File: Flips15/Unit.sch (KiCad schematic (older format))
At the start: 2 parts, among them U201 74LS138

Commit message: rework Flips15 draft
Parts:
- removed U201: 74LS138, SMD_Packages:SO-16-N, symbol 74xx_IEEE:74LS138
- added U201: 74HC238, Housings_SOIC:SOIC-16_3.9x9.9mm_Pitch1.27mm, symbol 74xx_IEEE:74HC238
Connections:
- net B0: now also U201.2 (A1)
- net B1: now also U201.3 (A2)
- net DATA: now also U201.1 (A0)
- net EN: now also U201.6 (G1)
- net GND: now also U201.4 (~G2A), U201.5 (~G2B), U201.8 (GND)
- net VCC: now also U201.16 (VCC)
- new net E0H: U201.14 (Y1)
- new net E0L: U201.15 (Y0)
- new net E1H: U201.12 (Y3)
- new net E1L: U201.13 (Y2)
- new net E2H: U201.10 (Y5)
- new net E2L: U201.11 (Y4)
- new net E3H: U201.7 (Y7)
- new net E3L: U201.9 (Y6)
- no-connect marks 4 -> 0

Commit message: more silk screen (use more compact IC values)
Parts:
- U201: value 74HC238 -> 74238
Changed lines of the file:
@@
 AR Path="/5C4DA960/5C55B425" Ref="U701"  Part="1"
 F 0 "U701" H 2700 5616 50  0000 C CNN
-F 1 "74HC238" H 2700 5525 50  0000 C CNN
+F 1 "74238" H 2700 5525 50  0000 C CNN
 F 2 "Housings_SOIC:SOIC-16_3.9x9.9mm_Pitch1.27mm" H 2700 5100 50  0001 C CNN
 F 3 "" H 2700 5100 50  0001 C CNN

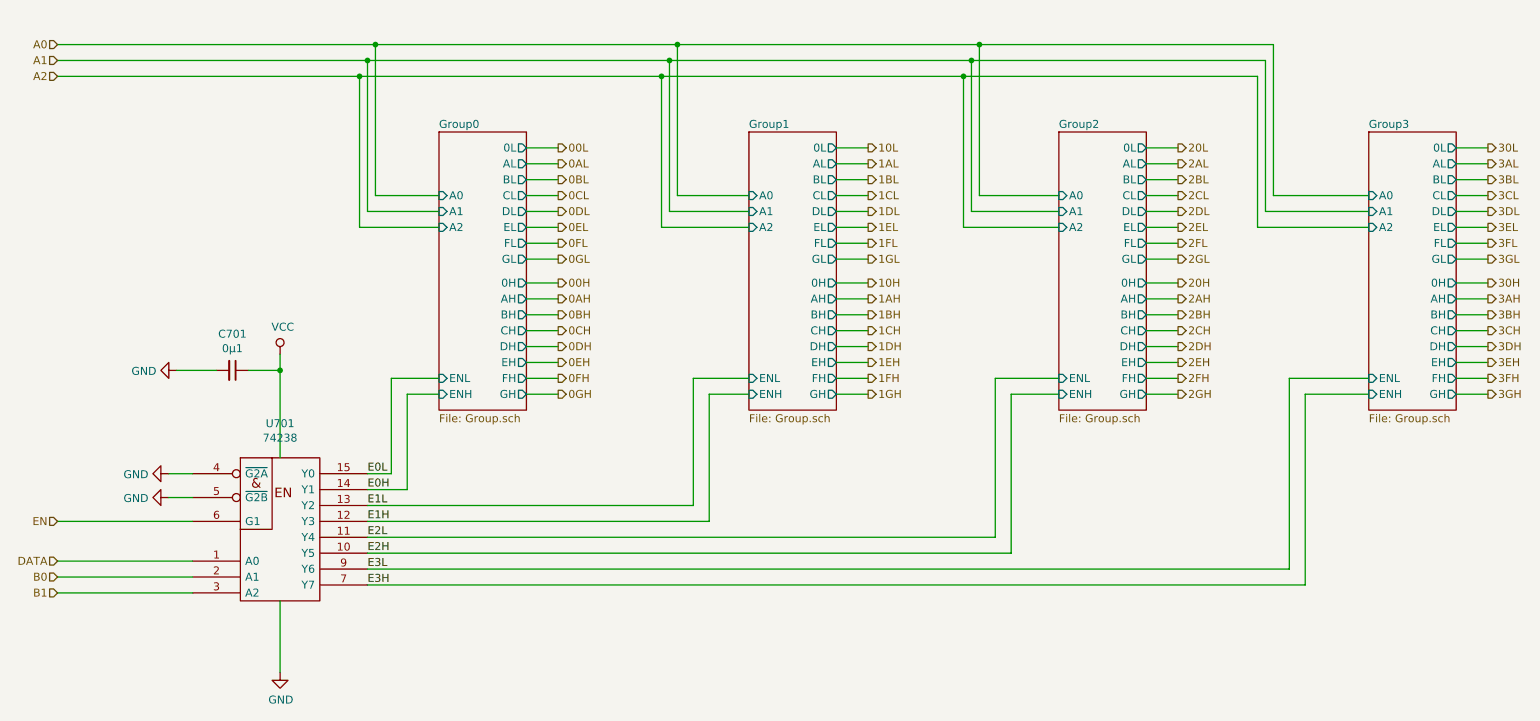
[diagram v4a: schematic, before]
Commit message: adding support for optional COM pin at BRDIC1
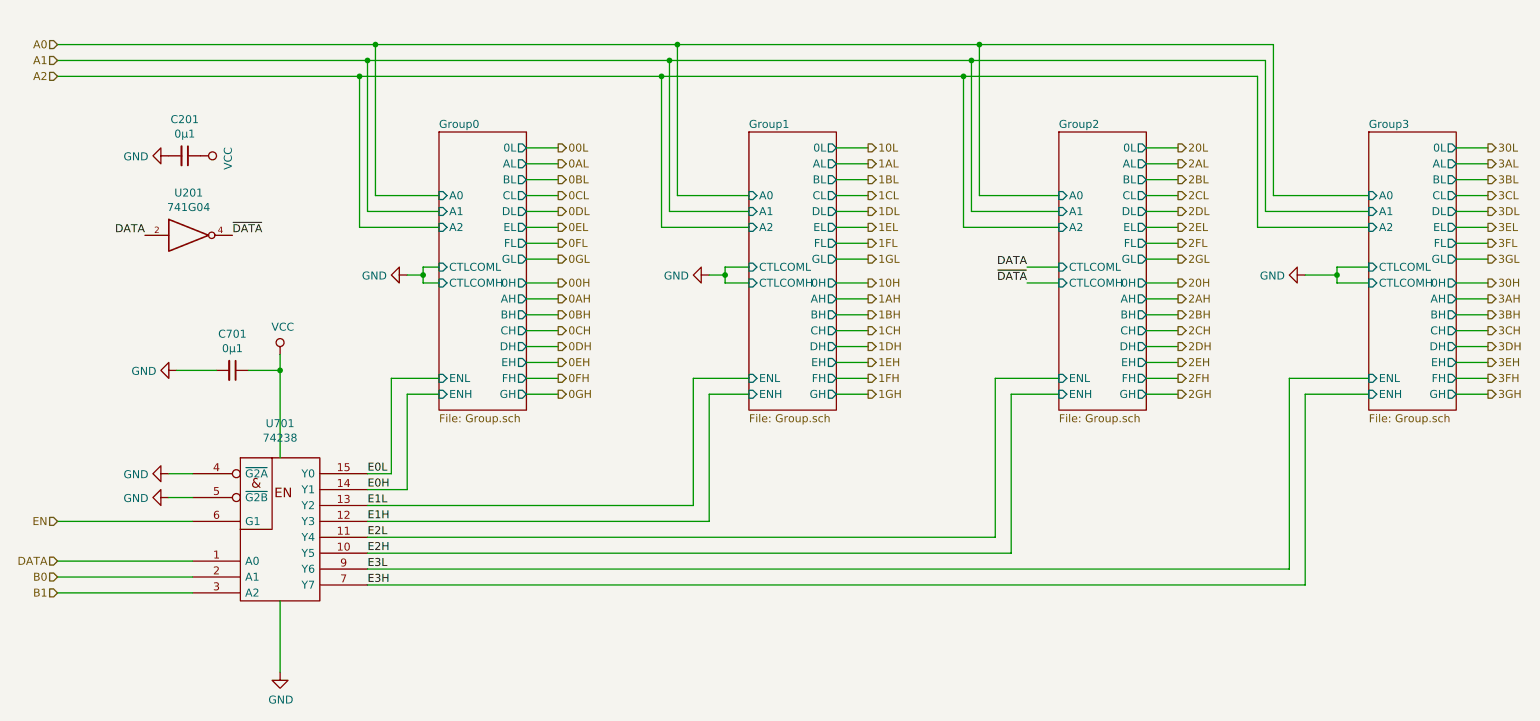
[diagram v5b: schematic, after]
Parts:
- added C201: 0μ1, Capacitors_SMD:C_0805_HandSoldering, symbol Device:C_Small
- added U201: 741G04, TO_SOT_Packages_SMD:SOT-23-5, symbol 74xGxx:74LVC1G04
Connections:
- net DATA: now also U201.2
- net GND: now also C201.2, U201.3 (GND)
- net VCC: now also C201.1, U201.5 (VCC)
- new net ~DATA: U201.4
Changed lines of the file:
@@
 F21 "ENH" I L 3700 4400 50
 F22 "ENL" I L 3700 4300 50
+F23 "CTLCOML" I L 3700 3600 50
+F24 "CTLCOMH" I L 3700 3700 50
 $EndSheet
 $Sheet
@@
 F21 "ENH" I L 5650 4400 50
 F22 "ENL" I L 5650 4300 50
+F23 "CTLCOML" I L 5650 3600 50
+F24 "CTLCOMH" I L 5650 3700 50
 $EndSheet
 $Sheet
@@
 F21 "ENH" I L 7600 4400 50
 F22 "ENL" I L 7600 4300 50
+F23 "CTLCOML" I L 7600 3600 50
+F24 "CTLCOMH" I L 7600 3700 50
 $EndSheet
 $Sheet
@@
 F21 "ENH" I L 9550 4400 50
 F22 "ENL" I L 9550 4300 50
+F23 "CTLCOML" I L 9550 3600 50
+F24 "CTLCOMH" I L 9550 3700 50
 $EndSheet
 Wire Wire Line
@@
 Text Label 3250 5600 0    50   ~ 0
 E3H
+$Comp
+L power:GND #PWR?
+U 1 1 5C5C466E
+P 3500 3650
+AR Path="/5C5C466E" Ref="#PWR?"  Part="1"
+AR Path="/5C4DA950/5C5C466E" Ref="#PWR?"  Part="1"
+AR Path="/5C4DA960/5C5C466E" Ref="#PWR0203"  Part="1"
+F 0 "#PWR0203" H 3500 3400 50  0001 C CNN
+F 1 "GND" V 3505 3522 50  0000 R CNN
+F 2 "" H 3500 3650 50  0001 C CNN
+F 3 "" H 3500 3650 50  0001 C CNN
+	1    3500 3650
+	0    1    1    0
+$EndComp
+Wire Wire Line
+	3500 3650 3600 3650
+Wire Wire Line
+	3600 3650 3600 3600
+Wire Wire Line
+	3600 3600 3700 3600
+Wire Wire Line
+	3700 3700 3600 3700
+Wire Wire Line
+	3600 3700 3600 3650
+Connection ~ 3600 3650
+Wire Wire Line
+	5650 3600 5500 3600
+Wire Wire Line
+	5500 3600 5500 3650
+Wire Wire Line
+	5500 3700 5650 3700
+Wire Wire Line
+	5500 3650 5400 3650
+Connection ~ 5500 3650
+Wire Wire Line
+	5500 3650 5500 3700
+$Comp
+L power:GND #PWR?
+U 1 1 5C5E08DC
+P 5400 3650
+AR Path="/5C5E08DC" Ref="#PWR?"  Part="1"
+AR Path="/5C4DA950/5C5E08DC" Ref="#PWR?"  Part="1"
+AR Path="/5C4DA960/5C5E08DC" Ref="#PWR0204"  Part="1"
+F 0 "#PWR0204" H 5400 3400 50  0001 C CNN
+F 1 "GND" V 5405 3522 50  0000 R CNN
+F 2 "" H 5400 3650 50  0001 C CNN
+F 3 "" H 5400 3650 50  0001 C CNN
+	1    5400 3650
+	0    1    1    0
+$EndComp
+Wire Wire Line
+	7400 3700 7600 3700
+Wire Wire Line
+	7600 3600 7400 3600
+Wire Wire Line
+	9550 3600 9350 3600
+Wire Wire Line
+	9350 3600 9350 3650
+Wire Wire Line
+	9350 3700 9550 3700
+Wire Wire Line
+	9350 3650 9150 3650
+Connection ~ 9350 3650
+Wire Wire Line
+	9350 3650 9350 3700
+$Comp
+L power:GND #PWR?
+U 1 1 5C5FF9CF
+P 9150 3650
+AR Path="/5C5FF9CF" Ref="#PWR?"  Part="1"
+AR Path="/5C4DA950/5C5FF9CF" Ref="#PWR?"  Part="1"
+AR Path="/5C4DA960/5C5FF9CF" Ref="#PWR0205"  Part="1"
+F 0 "#PWR0205" H 9150 3400 50  0001 C CNN
+F 1 "GND" V 9155 3522 50  0000 R CNN
+F 2 "" H 9150 3650 50  0001 C CNN
+F 3 "" H 9150 3650 50  0001 C CNN
+	1    9150 3650
+	0    1    1    0
+$EndComp
+Text Label 7400 3600 2    50   ~ 0
+DATA
+Text Label 7400 3700 2    50   ~ 0
+~DATA
+$Comp
+L 74xGxx:74LVC1G04 U201
+U 1 1 5C5FFB09
+P 2150 3400
+F 0 "U201" H 2125 3667 50  0000 C CNN
+F 1 "741G04" H 2125 3576 50  0000 C CNN
+F 2 "TO_SOT_Packages_SMD:SOT-23-5" H 2150 3400 50  0001 C CNN
+F 3 "http://www.ti.com/lit/sg/scyt129e/scyt129e.pdf" H 2150 3400 50  0001 C CNN
+	1    2150 3400
+	1    0    0    -1
+$EndComp
+Text Label 2400 3400 0    50   ~ 0
+~DATA
+Text Label 1850 3400 2    50   ~ 0
+DATA
+$Comp
+L Device:C_Small C?
+U 1 1 5C5FFCA0
+P 2100 2900
+AR Path="/5C4CE2B0/5C5FFCA0" Ref="C?"  Part="1"
+AR Path="/5C5018C5/5C5FFCA0" Ref="C?"  Part="1"
+AR Path="/5C5FFCA0" Ref="C?"  Part="1"
+AR Path="/5C4DA950/5C5FFCA0" Ref="C?"  Part="1"
+AR Path="/5C4DA960/5C5FFCA0" Ref="C201"  Part="1"
+F 0 "C201" V 1871 2900 50  0000 C CNN
+F 1 "0μ1" V 1962 2900 50  0000 C CNN
+F 2 "Capacitors_SMD:C_0805_HandSoldering" H 2100 2900 50  0001 C CNN
+F 3 "~" H 2100 2900 50  0001 C CNN
+	1    2100 2900
+	0    1    1    0
+$EndComp
+$Comp
+L power:GND #PWR?
+U 1 1 5C5FFCE8
+P 2000 2900
+AR Path="/5C5FFCE8" Ref="#PWR?"  Part="1"
+AR Path="/5C4DA950/5C5FFCE8" Ref="#PWR?"  Part="1"
+AR Path="/5C4DA960/5C5FFCE8" Ref="#PWR0201"  Part="1"
+F 0 "#PWR0201" H 2000 2650 50  0001 C CNN
+F 1 "GND" V 2005 2772 50  0000 R CNN
+F 2 "" H 2000 2900 50  0001 C CNN
+F 3 "" H 2000 2900 50  0001 C CNN
+	1    2000 2900
+	0    1    1    0
+$EndComp
+$Comp
+L power:VCC #PWR?
+U 1 1 5C5FFCFB
+P 2200 2900
+AR Path="/5C5FFCFB" Ref="#PWR?"  Part="1"
+AR Path="/5C4DA950/5C5FFCFB" Ref="#PWR?"  Part="1"
+AR Path="/5C4DA960/5C5FFCFB" Ref="#PWR0202"  Part="1"
+F 0 "#PWR0202" H 2200 2750 50  0001 C CNN
+F 1 "VCC" H 2217 3073 50  0000 C CNN
+F 2 "" H 2200 2900 50  0001 C CNN
+F 3 "" H 2200 2900 50  0001 C CNN
+	1    2200 2900
+	0    1    1    0
+$EndComp
 $EndSCHEMATC

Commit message: re-annotating to get more compact part numbers
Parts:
- renumbered C201 to C2, U201 to U2
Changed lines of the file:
@@
 AR Path="/5C5018C5/5C4DAB40" Ref="C?"  Part="1"
 AR Path="/5C4DAB40" Ref="C?"  Part="1"
-AR Path="/5C4DA950/5C4DAB40" Ref="C201"  Part="1"
-AR Path="/5C4DA960/5C4DAB40" Ref="C701"  Part="1"
-F 0 "C701" V 2171 4250 50  0000 C CNN
+AR Path="/5C4DA950/5C4DAB40" Ref="C2"  Part="1"
+AR Path="/5C4DA960/5C4DAB40" Ref="C1"  Part="1"
+F 0 "C1" V 2171 4250 50  0000 C CNN
 F 1 "0μ1" V 2262 4250 50  0000 C CNN
 F 2 "Capacitors_SMD:C_0805_HandSoldering" H 2400 4250 50  0001 C CNN
@@
 	9150 4400 9550 4400
 $Comp
-L 74xx_IEEE:74HC238 U201
+L 74xx_IEEE:74HC238 U2
 U 1 1 5C55B425
 P 2700 5100
-AR Path="/5C4DA950/5C55B425" Ref="U201"  Part="1"
-AR Path="/5C4DA960/5C55B425" Ref="U701"  Part="1"
-F 0 "U701" H 2700 5616 50  0000 C CNN
+AR Path="/5C4DA950/5C55B425" Ref="U2"  Part="1"
+AR Path="/5C4DA960/5C55B425" Ref="U1"  Part="1"
+F 0 "U1" H 2700 5616 50  0000 C CNN
 F 1 "74238" H 2700 5525 50  0000 C CNN
 F 2 "Housings_SOIC:SOIC-16_3.9x9.9mm_Pitch1.27mm" H 2700 5100 50  0001 C CNN
@@
 ~DATA
 $Comp
-L 74xGxx:74LVC1G04 U201
+L 74xGxx:74LVC1G04 U2
 U 1 1 5C5FFB09
 P 2150 3400
-F 0 "U201" H 2125 3667 50  0000 C CNN
+F 0 "U2" H 2125 3667 50  0000 C CNN
 F 1 "741G04" H 2125 3576 50  0000 C CNN
 F 2 "TO_SOT_Packages_SMD:SOT-23-5" H 2150 3400 50  0001 C CNN
@@
 AR Path="/5C5FFCA0" Ref="C?"  Part="1"
 AR Path="/5C4DA950/5C5FFCA0" Ref="C?"  Part="1"
-AR Path="/5C4DA960/5C5FFCA0" Ref="C201"  Part="1"
-F 0 "C201" V 1871 2900 50  0000 C CNN
+AR Path="/5C4DA960/5C5FFCA0" Ref="C2"  Part="1"
+F 0 "C2" V 1871 2900 50  0000 C CNN
 F 1 "0μ1" V 1962 2900 50  0000 C CNN
 F 2 "Capacitors_SMD:C_0805_HandSoldering" H 2100 2900 50  0001 C CNN
